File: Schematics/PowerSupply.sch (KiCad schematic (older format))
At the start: 11 parts, among them Q1 2N7000, U1 LM2576T-5, U2 LM1117-3.3

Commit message: Added BT module, HU-CDC interface adapter, I2S to SPDIF converter, SPDIF interface and main controller to the schematics
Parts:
- removed C3: 100nF, Capacitor_THT:C_Disc_D5.0mm_W2.5mm_P2.50mm, symbol Device:C
- removed C4: 10uF, Capacitor_THT:C_Disc_D5.0mm_W2.5mm_P2.50mm, symbol Device:C
- added C3: 10uF, Capacitor_THT:CP_Radial_Tantal_D5.0mm_P2.50mm, symbol Device:CP
- added C4: 100uF, Capacitor_THT:CP_Radial_D10.0mm_P5.00mm, symbol Device:CP
- Q1: Spice_Lib_File (none) -> /home/lengyela/Downloads/2N7000.REV0.LIB; Spice_Model (none) -> 2n7000; Spice_Netlist_Enabled (none) -> Y; Spice_Primitive (none) -> X
- U1: Spice_Lib_File (none) -> /home/lengyela/Downloads/LM2576_PSPICE_TRANS/LM2576_TRANS.L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; Spice_Model (none) -> LM2576_TRANS; Spice_Netlist_Enabled (none) -> N; Spice_Primitive (none) -> X
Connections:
- net labels added: PWR_ON
- wire segments 47 -> 48
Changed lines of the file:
@@
 $Descr A4 11693 8268
 encoding utf-8
-Sheet 2 2
+Sheet 2 8
 Title ""
 Date ""
@@
 AR Path="/5CC09295" Ref="U?"  Part="1"
 AR Path="/5CC08323/5CC09295" Ref="U1"  Part="1"
-F 0 "U1" H 5350 3567 50  0000 C CNN
-F 1 "LM2576T-5" H 5350 3476 50  0000 C CNN
+F 0 "U1" H 4950 3450 50  0000 L CNN
+F 1 "LM2576T-5" H 5350 3450 50  0000 L CNN
 F 2 "Package_TO_SOT_THT:TO-220-5_Vertical" H 5350 2950 50  0001 L CIN
 F 3 "http://www.ti.com/lit/ds/symlink/lm2576.pdf" H 5350 3200 50  0001 C CNN
+F 4 "X" H 5350 3200 50  0001 C CNN "Spice_Primitive"
+F 5 "LM2576_TRANS" H 5350 3200 50  0001 C CNN "Spice_Model"
+F 6 "N" H 5350 3200 50  0001 C CNN "Spice_Netlist_Enabled"
+F 7 "/home/lengyela/Downloads/LM2576_PSPICE_TRANS/LM2576_TRANS.LIB" H 5350 3200 50  0001 C CNN "Spice_Lib_File"
 	1    5350 3200
 	1    0    0    -1
@@
 	1    0    0    -1
 $EndComp
-$Comp
-L Transistor_FET:2N7000 Q?
-U 1 1 5CC092C5
-P 4350 4000
-AR Path="/5CC092C5" Ref="Q?"  Part="1"
-AR Path="/5CC08323/5CC092C5" Ref="Q1"  Part="1"
-F 0 "Q1" H 4555 4046 50  0000 L CNN
-F 1 "2N7000" H 4555 3955 50  0000 L CNN
-F 2 "Package_TO_SOT_THT:TO-92_Inline" H 4550 3925 50  0001 L CIN
-F 3 "https://www.fairchildsemi.com/datasheets/2N/2N7000.pdf" H 4350 4000 50  0001 L CNN
-	1    4350 4000
-	1    0    0    -1
-$EndComp
 Wire Wire Line
 	5850 3300 6000 3300
@@
 Wire Wire Line
 	7800 3900 7300 3900
-Connection ~ 6850 3900
-$Comp
-L Device:C C?
-U 1 1 5CC092DC
-P 7300 3550
-AR Path="/5CC092DC" Ref="C?"  Part="1"
-AR Path="/5CC08323/5CC092DC" Ref="C3"  Part="1"
-F 0 "C3" H 7415 3596 50  0000 L CNN
-F 1 "100nF" H 7415 3505 50  0000 L CNN
-F 2 "Capacitor_THT:C_Disc_D5.0mm_W2.5mm_P2.50mm" H 7338 3400 50  0001 C CNN
-F 3 "~" H 7300 3550 50  0001 C CNN
-	1    7300 3550
-	1    0    0    -1
-$EndComp
-$Comp
-L Device:C C?
-U 1 1 5CC092E3
-P 8300 3550
-AR Path="/5CC092E3" Ref="C?"  Part="1"
-AR Path="/5CC08323/5CC092E3" Ref="C4"  Part="1"
-F 0 "C4" H 8415 3596 50  0000 L CNN
-F 1 "10uF" H 8415 3505 50  0000 L CNN
-F 2 "Capacitor_THT:C_Disc_D5.0mm_W2.5mm_P2.50mm" H 8338 3400 50  0001 C CNN
-F 3 "~" H 8300 3550 50  0001 C CNN
-	1    8300 3550
-	1    0    0    -1
-$EndComp
 Wire Wire Line
 	7500 3100 7300 3100
 Wire Wire Line
 	7300 3400 7300 3100
-Connection ~ 7300 3100
-Wire Wire Line
-	7300 3100 7100 3100
 Wire Wire Line
 	7300 3700 7300 3900
-Connection ~ 7300 3900
-Wire Wire Line
-	7300 3900 6850 3900
 Wire Wire Line
 	8300 3400 8300 3100
@@
 	3850 3600 3850 4600
 Wire Wire Line
-	4800 3300 4800 3700
-Wire Wire Line
 	4450 3600 4450 3700
 Wire Wire Line
@@
 Wire Wire Line
 	7100 2750 7100 3100
-Connection ~ 7100 3100
 Wire Wire Line
 	7100 3100 6850 3100
@@
 Text HLabel 5350 4650 3    50   Input ~ 0
 GND
+$Comp
+L Transistor_FET:2N7000 Q?
+U 1 1 5CC092C5
+P 4350 4000
+AR Path="/5CC092C5" Ref="Q?"  Part="1"
+AR Path="/5CC08323/5CC092C5" Ref="Q1"  Part="1"
+F 0 "Q1" H 4555 4046 50  0000 L CNN
+F 1 "2N7000" H 4555 3955 50  0000 L CNN
+F 2 "Package_TO_SOT_THT:TO-92_Inline" H 4550 3925 50  0001 L CIN
+F 3 "https://www.fairchildsemi.com/datasheets/2N/2N7000.pdf" H 4350 4000 50  0001 L CNN
+F 4 "X" H 4350 4000 50  0001 C CNN "Spice_Primitive"
+F 5 "2n7000" H 4350 4000 50  0001 C CNN "Spice_Model"
+F 6 "Y" H 4350 4000 50  0001 C CNN "Spice_Netlist_Enabled"
+F 7 "/home/lengyela/Downloads/2N7000.REV0.LIB" H 4350 4000 50  0001 C CNN "Spice_Lib_File"
+	1    4350 4000
+	1    0    0    -1
+$EndComp
+Text GLabel 3400 3700 0    50   Output ~ 0
+PWR_ON
+Wire Wire Line
+	6850 3900 7300 3900
+Connection ~ 6850 3900
+Connection ~ 7300 3900
+Wire Wire Line
+	7300 3100 7100 3100
+Connection ~ 7300 3100
+Connection ~ 7100 3100
+$Comp
+L Device:CP C3
+U 1 1 5CC77333
+P 7300 3550
+F 0 "C3" H 7418 3596 50  0000 L CNN
+F 1 "10uF" H 7418 3505 50  0000 L CNN
+F 2 "Capacitor_THT:CP_Radial_Tantal_D5.0mm_P2.50mm" H 7338 3400 50  0001 C CNN
+F 3 "~" H 7300 3550 50  0001 C CNN
+	1    7300 3550
+	1    0    0    -1
+$EndComp
+$Comp
+L Device:CP C4
+U 1 1 5CC773D4
+P 8300 3550
+F 0 "C4" H 8418 3596 50  0000 L CNN
+F 1 "100uF" H 8418 3505 50  0000 L CNN
+F 2 "Capacitor_THT:CP_Radial_D10.0mm_P5.00mm" H 8338 3400 50  0001 C CNN
+F 3 "~" H 8300 3550 50  0001 C CNN
+	1    8300 3550
+	1    0    0    -1
+$EndComp
+Wire Wire Line
+	3400 3700 4450 3700
+Wire Wire Line
+	4800 3300 4800 3700
 $EndSCHEMATC

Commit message: Modified power supply
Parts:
- removed D1: 1N5822, Diode_THT:D_DO-201AD_P15.24mm_Horizontal, symbol Diode:1N5822
- removed U1: LM2576T-5, Package_TO_SOT_THT:TO-220-5_Vertical, symbol Regulator_Switching:LM2576T-5
- added D1: 1N5819, Diode_THT:D_DO-41_SOD81_P10.16mm_Horizontal, symbol Diode:1N5819
- added U1: LM2575-5.0BT, Package_TO_SOT_THT:TO-220-5_Vertical, symbol Regulator_Switching:LM2575-5.0BT
- C2: value 1000uF -> 330uF
- L1: value 100uH -> 330uH
- R1, R2: value 20K -> 10K
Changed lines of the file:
@@
 $EndDescr
-$Comp
-L Regulator_Switching:LM2576T-5 U?
-U 1 1 5CC09295
-P 5350 3200
-AR Path="/5CC09295" Ref="U?"  Part="1"
-AR Path="/5CC08323/5CC09295" Ref="U1"  Part="1"
-F 0 "U1" H 4950 3450 50  0000 L CNN
-F 1 "LM2576T-5" H 5350 3450 50  0000 L CNN
-F 2 "Package_TO_SOT_THT:TO-220-5_Vertical" H 5350 2950 50  0001 L CIN
-F 3 "http://www.ti.com/lit/ds/symlink/lm2576.pdf" H 5350 3200 50  0001 C CNN
-F 4 "X" H 5350 3200 50  0001 C CNN "Spice_Primitive"
-F 5 "LM2576_TRANS" H 5350 3200 50  0001 C CNN "Spice_Model"
-F 6 "N" H 5350 3200 50  0001 C CNN "Spice_Netlist_Enabled"
-F 7 "/home/lengyela/Downloads/LM2576_PSPICE_TRANS/LM2576_TRANS.LIB" H 5350 3200 50  0001 C CNN "Spice_Lib_File"
-	1    5350 3200
-	1    0    0    -1
-$EndComp
 $Comp
 L Regulator_Linear:LM1117-3.3 U?
@@
 AR Path="/5CC08323/5CC092AA" Ref="C2"  Part="1"
 F 0 "C2" H 6968 3596 50  0000 L CNN
-F 1 "1000uF" H 6968 3505 50  0000 L CNN
+F 1 "330uF" H 6968 3505 50  0000 L CNN
 F 2 "Capacitor_THT:CP_Radial_D10.0mm_P5.00mm" H 6888 3400 50  0001 C CNN
 F 3 "~" H 6850 3550 50  0001 C CNN
 	1    6850 3550
 	1    0    0    -1
-$EndComp
-$Comp
-L Diode:1N5822 D?
-U 1 1 5CC092B1
-P 6000 3550
-AR Path="/5CC092B1" Ref="D?"  Part="1"
-AR Path="/5CC08323/5CC092B1" Ref="D1"  Part="1"
-F 0 "D1" V 5954 3629 50  0000 L CNN
-F 1 "1N5822" V 6045 3629 50  0000 L CNN
-F 2 "Diode_THT:D_DO-201AD_P15.24mm_Horizontal" H 6000 3375 50  0001 C CNN
-F 3 "http://www.vishay.com/docs/88526/1n5820.pdf" H 6000 3550 50  0001 C CNN
-	1    6000 3550
-	0    1    1    0
 $EndComp
 $Comp
@@
 AR Path="/5CC08323/5CC092B8" Ref="L1"  Part="1"
 F 0 "L1" H 6350 3515 50  0000 C CNN
-F 1 "100uH" H 6350 3424 50  0000 C CNN
+F 1 "330uH" H 6350 3424 50  0000 C CNN
 F 2 "Inductor_THT:L_Radial_D10.0mm_P5.00mm_Fastron_07M" H 6350 3300 50  0001 C CNN
 F 3 "" H 6350 3300 50  0001 C CNN
@@
 AR Path="/5CC08323/5CC092F6" Ref="R2"  Part="1"
 F 0 "R2" V 4243 3450 50  0000 C CNN
-F 1 "20K" V 4334 3450 50  0000 C CNN
+F 1 "10K" V 4334 3450 50  0000 C CNN
 F 2 "Resistor_THT:R_Axial_DIN0207_L6.3mm_D2.5mm_P10.16mm_Horizontal" V 4380 3450 50  0001 C CNN
 F 3 "~" H 4450 3450 50  0001 C CNN
@@
 AR Path="/5CC08323/5CC09303" Ref="R1"  Part="1"
 F 0 "R1" H 4120 4346 50  0000 L CNN
-F 1 "20K" H 4120 4255 50  0000 L CNN
+F 1 "10K" H 4120 4255 50  0000 L CNN
 F 2 "Resistor_THT:R_Axial_DIN0207_L6.3mm_D2.5mm_P10.16mm_Horizontal" V 3980 4300 50  0001 C CNN
 F 3 "~" H 4050 4300 50  0001 C CNN
@@
 Wire Wire Line
 	4800 3300 4800 3700
+$Comp
+L Regulator_Switching:LM2575-5.0BT U1
+U 1 1 5D11C563
+P 5350 3200
+F 0 "U1" H 5350 3567 50  0000 C CNN
+F 1 "LM2575-5.0BT" H 5350 3476 50  0000 C CNN
+F 2 "Package_TO_SOT_THT:TO-220-5_Vertical" H 5350 2950 50  0001 L CIN
+F 3 "http://ww1.microchip.com/downloads/en/DeviceDoc/lm2575.pdf" H 5350 3200 50  0001 C CNN
+	1    5350 3200
+	1    0    0    -1
+$EndComp
+$Comp
+L Diode:1N5819 D1
+U 1 1 5D11C75B
+P 6000 3550
+F 0 "D1" V 5954 3629 50  0000 L CNN
+F 1 "1N5819" V 6045 3629 50  0000 L CNN
+F 2 "Diode_THT:D_DO-41_SOD81_P10.16mm_Horizontal" H 6000 3375 50  0001 C CNN
+F 3 "http://www.vishay.com/docs/88525/1n5817.pdf" H 6000 3550 50  0001 C CNN
+	1    6000 3550
+	0    1    1    0
+$EndComp
 $EndSCHEMATC

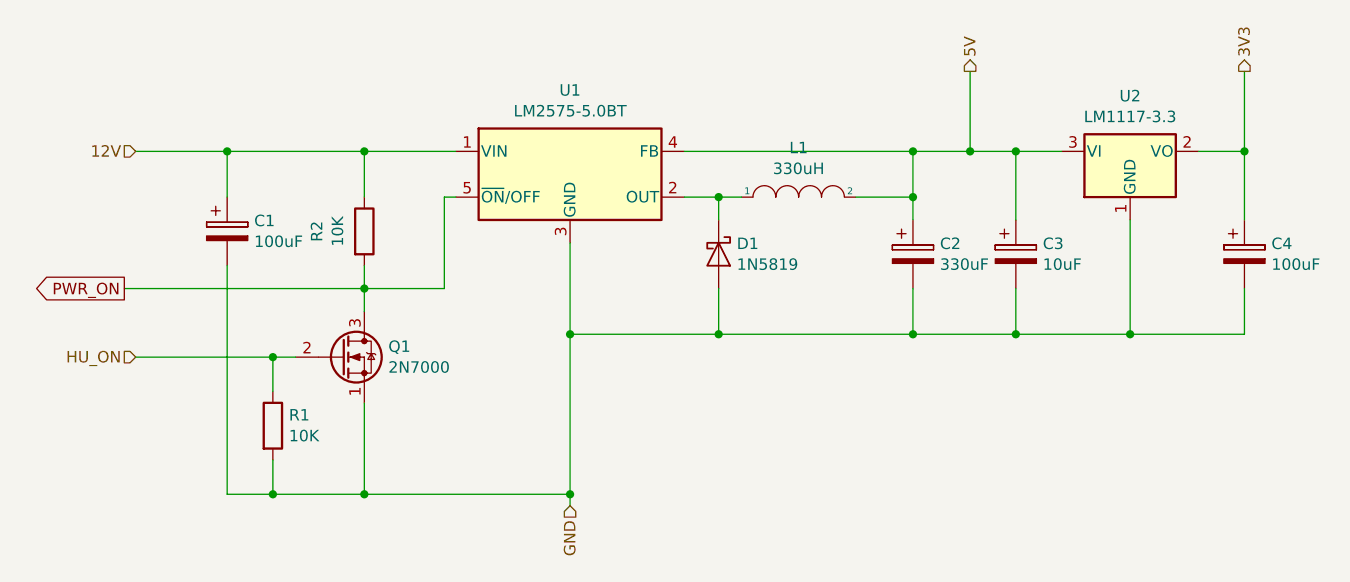
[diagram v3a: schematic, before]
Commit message: Added foorprint for screw terminals; simplified power supply; PCB partial design
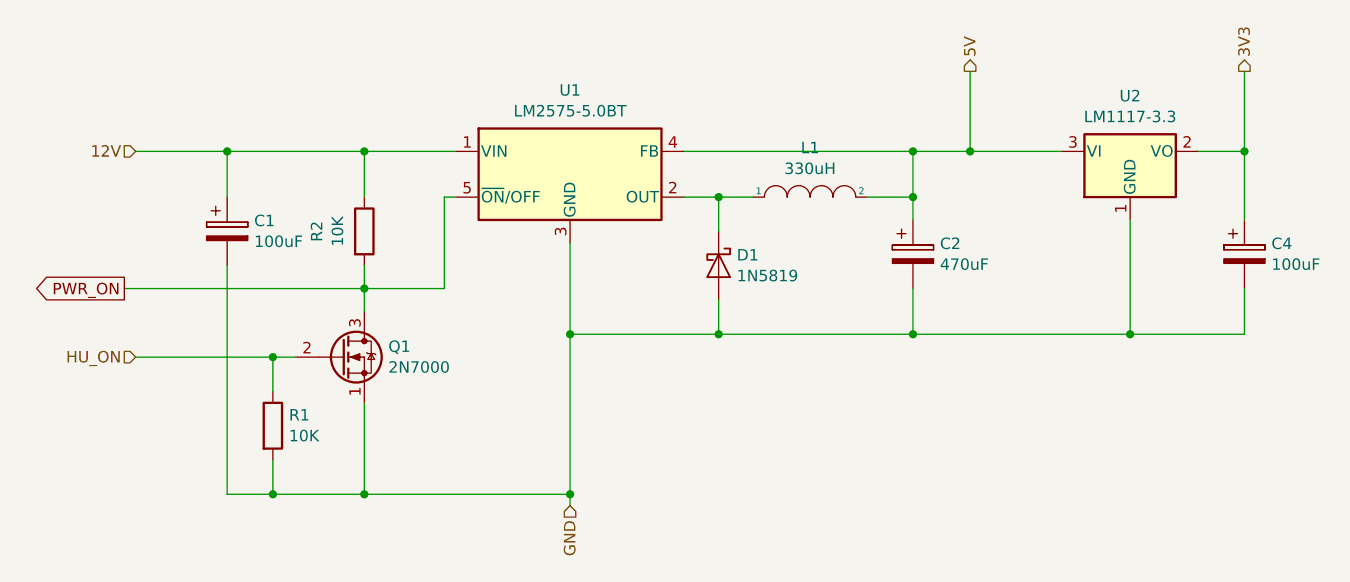
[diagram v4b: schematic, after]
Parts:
- removed C3: 10uF, Capacitor_THT:CP_Radial_Tantal_D5.0mm_P2.50mm, symbol Device:CP
- C2: value 330uF -> 470uF
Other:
- moved on the sheet: D1, L1
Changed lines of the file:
@@
 AR Path="/5CC08323/5CC092AA" Ref="C2"  Part="1"
 F 0 "C2" H 6968 3596 50  0000 L CNN
-F 1 "330uF" H 6968 3505 50  0000 L CNN
+F 1 "470uF" H 6968 3505 50  0000 L CNN
 F 2 "Capacitor_THT:CP_Radial_D10.0mm_P5.00mm" H 6888 3400 50  0001 C CNN
 F 3 "~" H 6850 3550 50  0001 C CNN
@@
 L pspice:INDUCTOR L?
 U 1 1 5CC092B8
-P 6350 3300
+P 6400 3300
 AR Path="/5CC092B8" Ref="L?"  Part="1"
 AR Path="/5CC08323/5CC092B8" Ref="L1"  Part="1"
-F 0 "L1" H 6350 3515 50  0000 C CNN
-F 1 "330uH" H 6350 3424 50  0000 C CNN
-F 2 "Inductor_THT:L_Radial_D10.0mm_P5.00mm_Fastron_07M" H 6350 3300 50  0001 C CNN
-F 3 "" H 6350 3300 50  0001 C CNN
-	1    6350 3300
+F 0 "L1" H 6400 3515 50  0000 C CNN
+F 1 "330uH" H 6400 3424 50  0000 C CNN
+F 2 "Inductor_THT:L_Radial_D10.0mm_P5.00mm_Fastron_07M" H 6400 3300 50  0001 C CNN
+F 3 "" H 6400 3300 50  0001 C CNN
+	1    6400 3300
 	1    0    0    -1
 $EndComp
@@
 	5850 3300 6000 3300
 Wire Wire Line
-	6000 3400 6000 3300
+	6000 3450 6000 3300
 Connection ~ 6000 3300
 Wire Wire Line
-	6000 3300 6100 3300
-Wire Wire Line
-	6600 3300 6850 3300
+	6000 3300 6150 3300
+Wire Wire Line
+	6650 3300 6850 3300
 Wire Wire Line
 	6850 3300 6850 3400
 Wire Wire Line
-	6000 3700 6000 3900
+	6000 3750 6000 3900
 Wire Wire Line
 	6850 3700 6850 3900
@@
 Wire Wire Line
 	7800 3400 7800 3900
-Wire Wire Line
-	7800 3900 7300 3900
-Wire Wire Line
-	7500 3100 7300 3100
-Wire Wire Line
-	7300 3400 7300 3100
-Wire Wire Line
-	7300 3700 7300 3900
 Wire Wire Line
 	8300 3400 8300 3100
@@
 Text GLabel 3400 3700 0    50   Output ~ 0
 PWR_ON
-Wire Wire Line
-	6850 3900 7300 3900
 Connection ~ 6850 3900
-Connection ~ 7300 3900
-Wire Wire Line
-	7300 3100 7100 3100
-Connection ~ 7300 3100
 Connection ~ 7100 3100
-$Comp
-L Device:CP C3
-U 1 1 5CC77333
-P 7300 3550
-F 0 "C3" H 7418 3596 50  0000 L CNN
-F 1 "10uF" H 7418 3505 50  0000 L CNN
-F 2 "Capacitor_THT:CP_Radial_Tantal_D5.0mm_P2.50mm" H 7338 3400 50  0001 C CNN
-F 3 "~" H 7300 3550 50  0001 C CNN
-	1    7300 3550
-	1    0    0    -1
-$EndComp
 $Comp
 L Device:CP C4
@@
 L Diode:1N5819 D1
 U 1 1 5D11C75B
-P 6000 3550
-F 0 "D1" V 5954 3629 50  0000 L CNN
-F 1 "1N5819" V 6045 3629 50  0000 L CNN
-F 2 "Diode_THT:D_DO-41_SOD81_P10.16mm_Horizontal" H 6000 3375 50  0001 C CNN
-F 3 "http://www.vishay.com/docs/88525/1n5817.pdf" H 6000 3550 50  0001 C CNN
-	1    6000 3550
+P 6000 3600
+F 0 "D1" V 5954 3679 50  0000 L CNN
+F 1 "1N5819" V 6045 3679 50  0000 L CNN
+F 2 "Diode_THT:D_DO-41_SOD81_P10.16mm_Horizontal" H 6000 3425 50  0001 C CNN
+F 3 "http://www.vishay.com/docs/88525/1n5817.pdf" H 6000 3600 50  0001 C CNN
+	1    6000 3600
 	0    1    1    0
 $EndComp
+Wire Wire Line
+	6850 3900 7800 3900
+Wire Wire Line
+	7100 3100 7500 3100
 $EndSCHEMATC

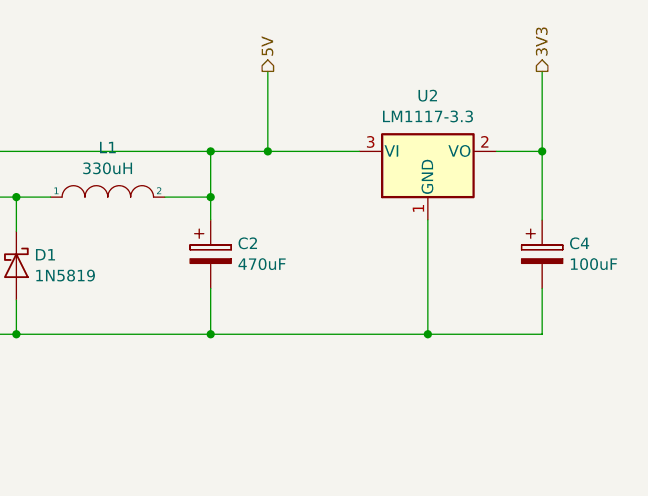
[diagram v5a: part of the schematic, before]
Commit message: Modified power supply schematic and PCB design; added new library for lm3940 IC.
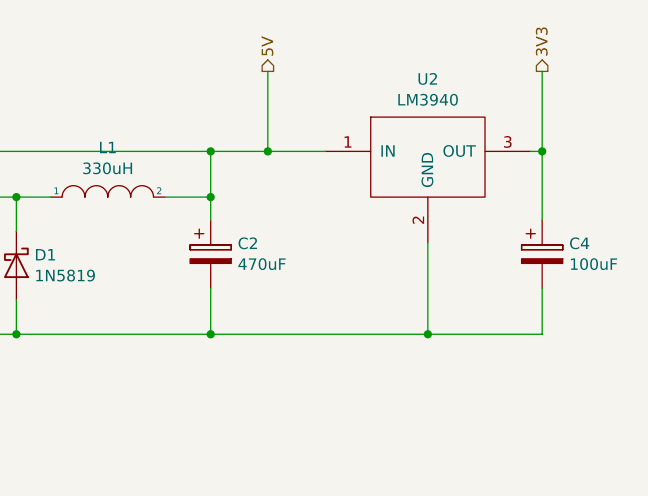
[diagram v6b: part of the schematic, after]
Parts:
- removed U2: LM1117-3.3, Package_TO_SOT_THT:TO-220-3_Vertical, symbol Regulator_Linear:LM1117-3.3
- added U2: LM3940, Package_TO_SOT_THT:TO-220-3_Vertical, symbol LM3940:LM3940
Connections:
- net 3V3: now also U2.3 (OUT)
- net 5V: now also U2.1 (IN)
- net GND: now also U2.2 (GND)
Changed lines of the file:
@@
 $EndDescr
-$Comp
-L Regulator_Linear:LM1117-3.3 U?
-U 1 1 5CC0929C
-P 7800 3100
-AR Path="/5CC0929C" Ref="U?"  Part="1"
-AR Path="/5CC08323/5CC0929C" Ref="U2"  Part="1"
-F 0 "U2" H 7800 3342 50  0000 C CNN
-F 1 "LM1117-3.3" H 7800 3251 50  0000 C CNN
-F 2 "Package_TO_SOT_THT:TO-220-3_Vertical" H 7800 3100 50  0001 C CNN
-F 3 "http://www.ti.com/lit/ds/symlink/lm1117.pdf" H 7800 3100 50  0001 C CNN
-	1    7800 3100
-	1    0    0    -1
-$EndComp
 $Comp
 L Device:CP C?
@@
 Connection ~ 6850 3100
 Wire Wire Line
-	7800 3400 7800 3900
-Wire Wire Line
 	8300 3400 8300 3100
 Wire Wire Line
-	8300 3100 8100 3100
+	8300 3100 8250 3100
 Wire Wire Line
 	8300 3700 8300 3900
@@
 PWR_ON
 Connection ~ 6850 3900
-Connection ~ 7100 3100
 $Comp
 L Device:CP C4
@@
 	6850 3900 7800 3900
 Wire Wire Line
-	7100 3100 7500 3100
+	7100 3100 7350 3100
+Connection ~ 7100 3100
+Wire Wire Line
+	7800 3500 7800 3900
+$Comp
+L LM3940:LM3940 U2
+U 1 1 5D31086E
+P 7800 3100
+F 0 "U2" H 7800 3415 50  0000 C CNN
+F 1 "LM3940" H 7800 3324 50  0000 C CNN
+F 2 "Package_TO_SOT_THT:TO-220-3_Vertical" H 7750 3100 50  0001 C CNN
+F 3 "" H 7750 3100 50  0001 C CNN
+	1    7800 3100
+	1    0    0    -1
+$EndComp
 $EndSCHEMATC

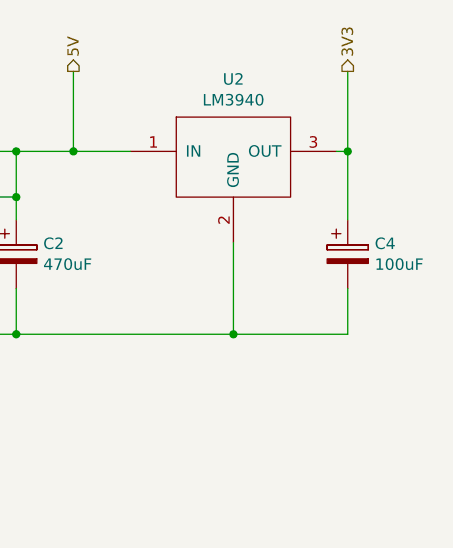
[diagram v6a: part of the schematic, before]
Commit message: Modified power supply schematic: changed C4 output capacitor to 470uF
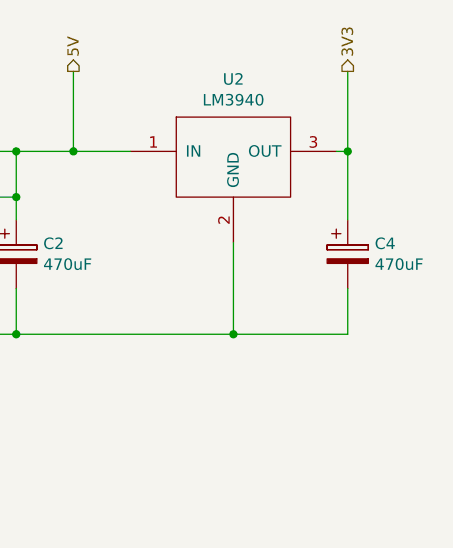
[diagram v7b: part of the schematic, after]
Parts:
- C4: value 100uF -> 470uF; footprint Capacitor_THT:CP_Radial_D10.0mm_P5.00mm -> Capacitor_THT:CP_Radial_D8.0mm_P3.50mm
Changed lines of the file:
@@
 EESchema Schematic File Version 4
 LIBS:RenaultBT-cache
-EELAYER 26 0
+EELAYER 29 0
 EELAYER END
 $Descr A4 11693 8268
@@
 P 8300 3550
 F 0 "C4" H 8418 3596 50  0000 L CNN
-F 1 "100uF" H 8418 3505 50  0000 L CNN
-F 2 "Capacitor_THT:CP_Radial_D10.0mm_P5.00mm" H 8338 3400 50  0001 C CNN
+F 1 "470uF" H 8418 3505 50  0000 L CNN
+F 2 "Capacitor_THT:CP_Radial_D8.0mm_P3.50mm" H 8338 3400 50  0001 C CNN
 F 3 "~" H 8300 3550 50  0001 C CNN
 	1    8300 3550
